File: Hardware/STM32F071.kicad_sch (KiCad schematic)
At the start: 1 part, among them U1 STM32C071K8Tx

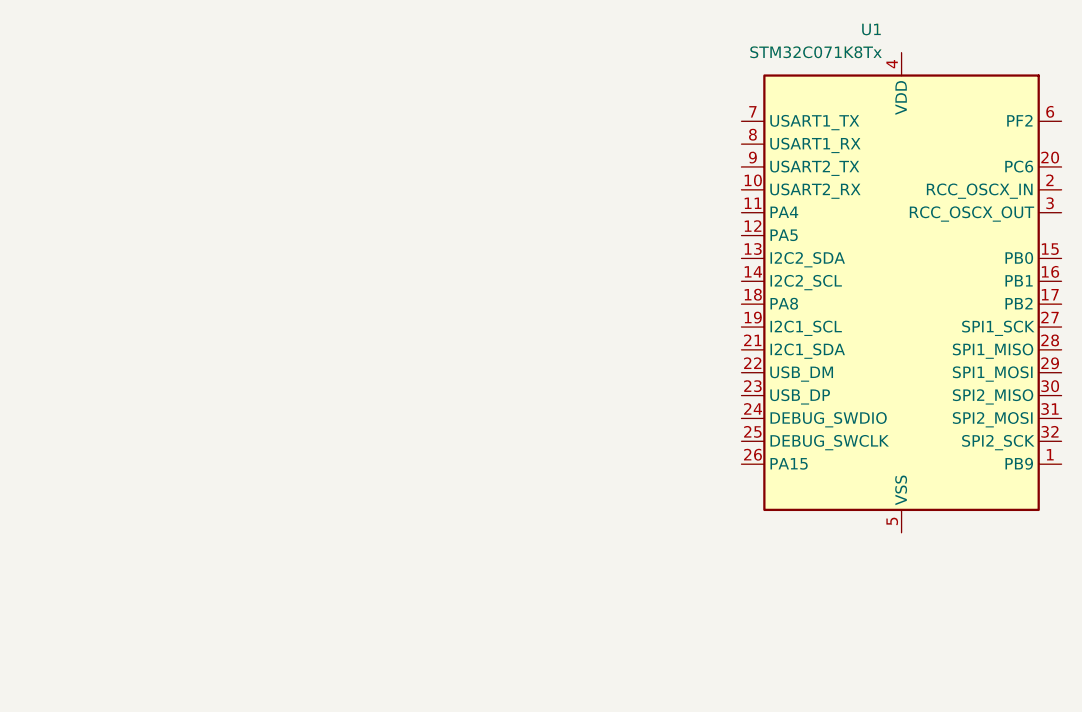
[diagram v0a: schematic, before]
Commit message: Added libraries, CPU and USB hookup
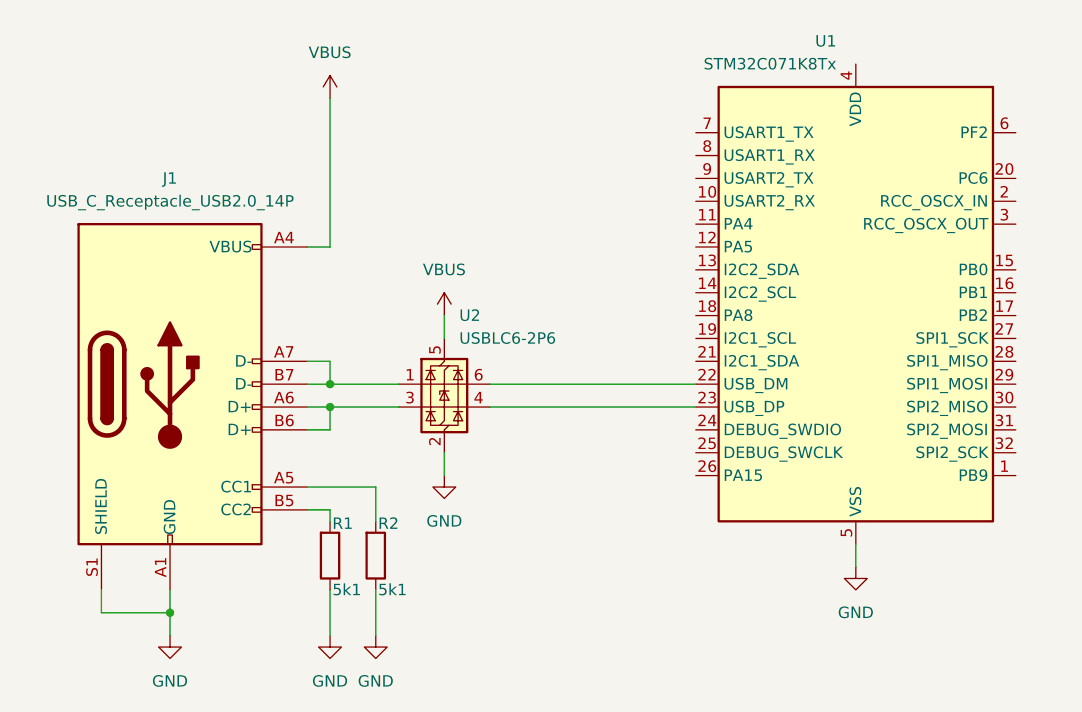
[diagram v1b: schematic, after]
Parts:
- added J1: USB_C_Receptacle_USB2.0_14P, project:USB-C_SMD-TYPE-C-31-M-12, symbol Connector:USB_C_Receptacle_USB2.0_14P
- added R1, R2: 5k1, symbol Device:R
- added U2: USBLC6-2P6, Package_TO_SOT_SMD:SOT-666, symbol Power_Protection:USBLC6-2P6
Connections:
- net at U1.22 (PA11): now also U2.6 (I/O1)
- net at U1.23 (PA12): now also U2.4 (I/O2)
- net GND: now reaches U1.5 (VSS)
- net GND: now also J1.A1 (GND), J1.A12 (GND), J1.B1 (GND), J1.B12 (GND), J1.S1 (SHIELD), R1.1, R2.1, U2.2 (GND)
- new net: J1.A5 (CC1), R2.2
- new net: J1.A6 (D+), J1.B6 (D+), U2.3 (I/O2)
- new net: J1.A7 (D-), J1.B7 (D-), U2.1 (I/O1)
- new net: J1.B5 (CC2), R1.2
- new net VBUS: J1.A4 (VBUS), J1.A9 (VBUS), J1.B4 (VBUS), J1.B9 (VBUS), U2.5 (VBUS)
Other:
- moved on the sheet: U1
